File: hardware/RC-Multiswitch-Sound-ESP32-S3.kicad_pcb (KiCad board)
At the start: 2 copper layers, 124 x 60.1 mm, 37 parts, among them CN1 UART A, CN2 3S, CN4 Lautsprecher, J1 Ausgaenge, J11 TPA3118 HW-327, J2 PCM5102A, J5 UART B, J6 UART C, J9 microSD-TF-Modul, U1 ESP32-S3-DevKitC-1 (N16R8), U2 ULN2803A

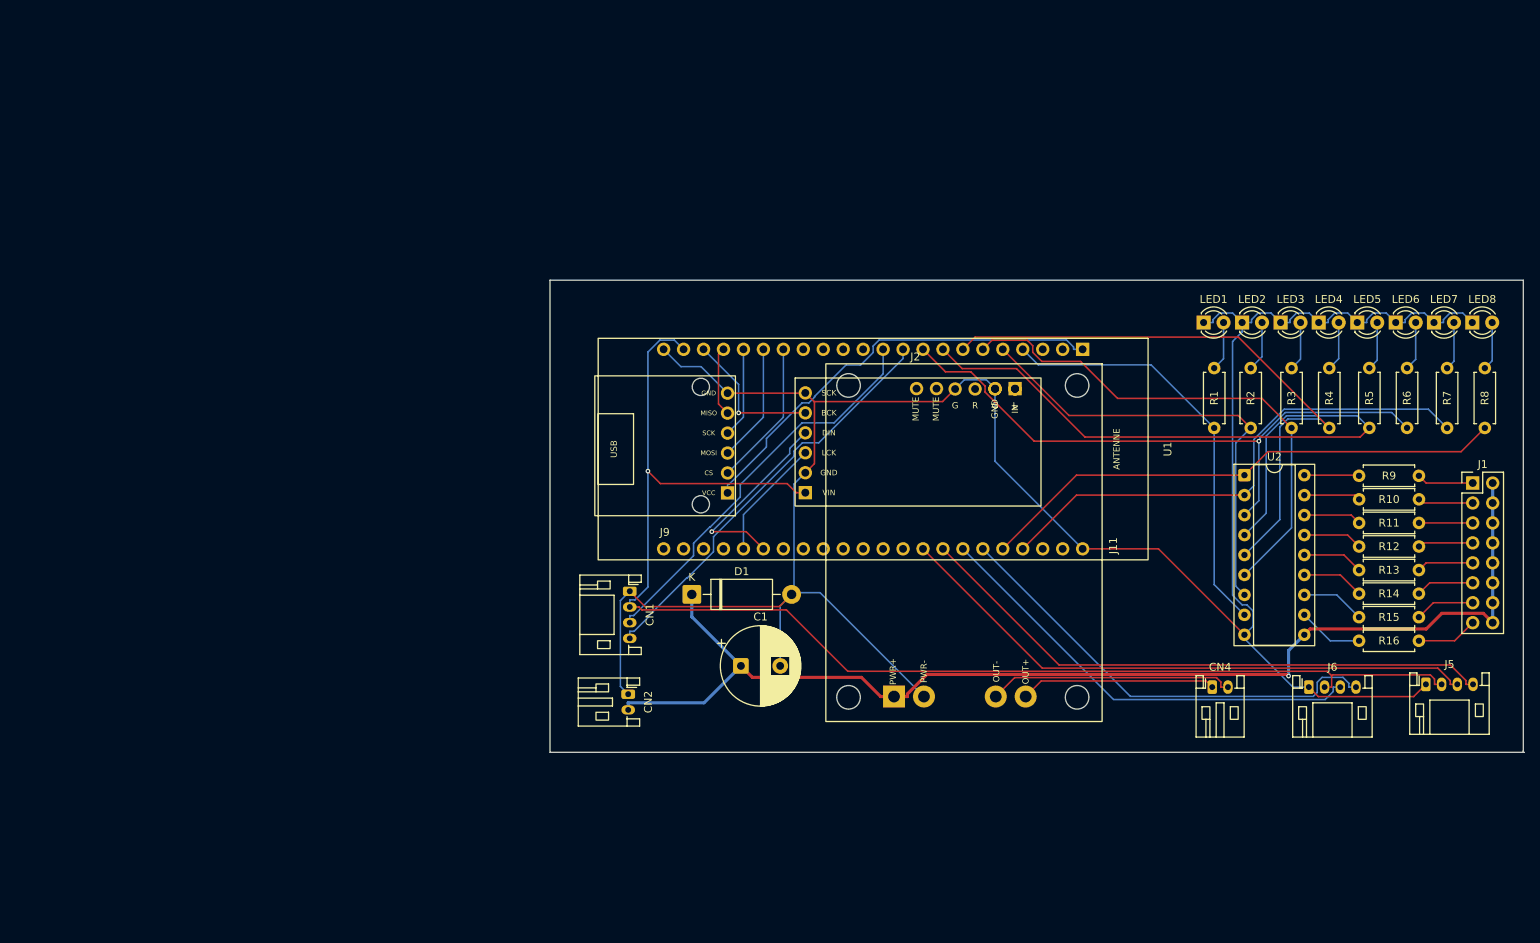
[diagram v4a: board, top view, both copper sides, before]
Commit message: PR #4 rückgängig: PCB wieder auf Stand vor VLOAD 0,4 mm
Auf Wunsch von Martin zurückgenommen.

Co-Authored-By: Claude Opus 5.5 (1M context) <noreply@anthropic.com>
Claude-Session: https://claude.ai/code/session_018bh1aktNNbeTvdMLiwxhbB
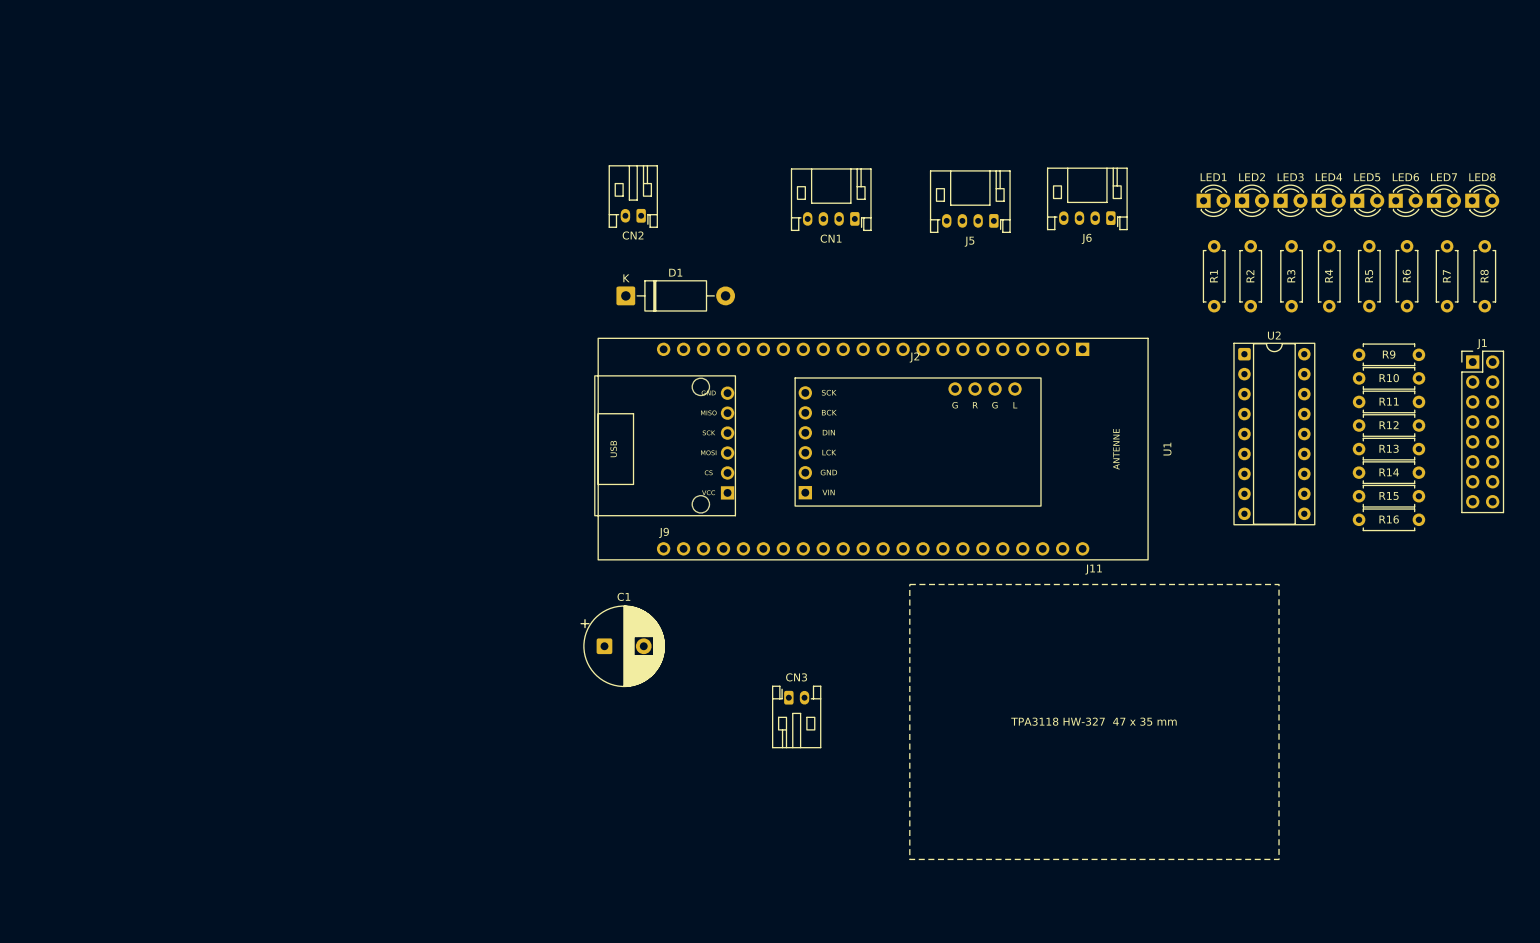
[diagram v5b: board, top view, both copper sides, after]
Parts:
- removed CN4: Lautsprecher, Connector_JST:JST_PH_S2B-PH-K_1x02_P2.00mm_Horizontal
- added CN3: TPA3118, Connector_JST:JST_PH_S2B-PH-K_1x02_P2.00mm_Horizontal, F.Cu at (176.2, 126.5)
- CN2: value 3S -> 12V
- D1: value P6KE15A -> P6KE33A
- J11: value TPA3118 HW-327 -> TPA3118 IN; footprint ESP32-S3-DevKitC-1_THT:Mod_TPA3118_HW327_THT -> ESP32-S3-DevKitC-1_THT:Mod_TPA3118_HW327_Keepout
- moved J5 80.7 mm to (202.3, 65.8), turned to 180 degrees
- moved J6 64.8 mm to (217.2, 65.4), turned to 180 degrees
- moved CN2 60.9 mm to (157.4, 65.1), turned to 180 degrees
- moved CN1 55.4 mm to (184.6, 65.5), turned to 180 degrees
- moved J11 43.6 mm to (215.1, 129.5), turned to 0 degrees
- moved D1 38.9 mm to (155.4, 75.3)
- moved C1 17.5 mm to (152.7, 119.9)
- moved LED1 15.5 mm to (229.0, 63.2)
- moved LED2 15.5 mm to (233.9, 63.2)
- moved LED3 15.5 mm to (238.8, 63.2)
- moved LED4 15.5 mm to (243.7, 63.2)
- moved LED5 15.5 mm to (248.6, 63.2)
- moved LED6 15.5 mm to (253.5, 63.2)
- moved LED7 15.5 mm to (258.3, 63.2)
- moved LED8 15.5 mm to (263.2, 63.2)
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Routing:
- net GND: track 302.5 -> 0.00 mm
- net +5V: track 170.9 -> 0.00 mm, vias 1 -> 0
- net /VLOAD: track 151.1 -> 0.00 mm, vias 1 -> 0
- net /S4: track 88.0 -> 0.00 mm
- net /S5: track 79.6 -> 0.00 mm, vias 1 -> 0
- net /S3: track 77.4 -> 0.00 mm
- net /UB_TX: track 75.5 -> 0.00 mm
- net /UB_RX: track 74.9 -> 0.00 mm
- net /S7: track 67.7 -> 0.00 mm
- net /S2: track 66.1 -> 0.00 mm
- net /S6: track 65.8 -> 0.00 mm
- net /S1: track 58.2 -> 0.00 mm
- net /UC_RX: track 57.9 -> 0.00 mm
- net /UC_TX: track 57.0 -> 0.00 mm
- net +3V3: track 55.8 -> 0.00 mm
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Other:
- board outline removed

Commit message: PCB: Platzierung/Routing von Martin (lokaler Stand), ERC-Bericht v0.9
Co-Authored-By: Claude Opus 5.5 (1M context) <noreply@anthropic.com>
Claude-Session: https://claude.ai/code/session_018bh1aktNNbeTvdMLiwxhbB
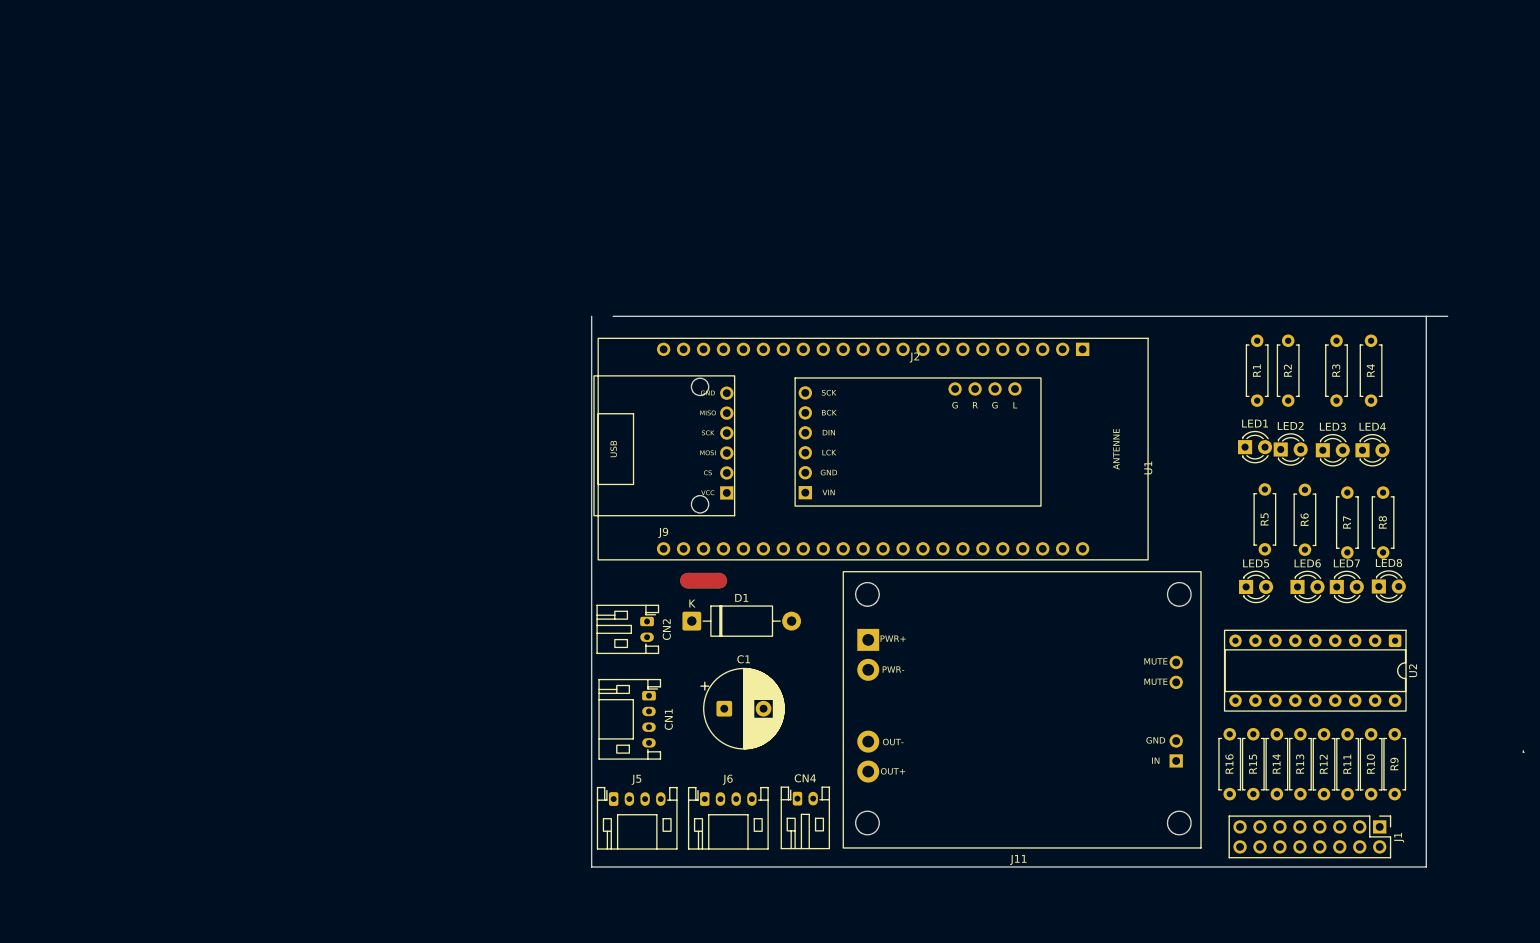
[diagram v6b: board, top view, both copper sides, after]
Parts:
- removed CN3: TPA3118, Connector_JST:JST_PH_S2B-PH-K_1x02_P2.00mm_Horizontal
- added CN4: Lautsprecher, Connector_JST:JST_PH_S2B-PH-K_1x02_P2.00mm_Horizontal, F.Cu at (177.3, 139.3)
- added NT1: NetTie GND/GNDPWR, NetTie:NetTie-2_SMD_Pad2.0mm, F.Cu at (165.3, 111.5)
- CN2: value 12V -> 3S
- D1: value P6KE33A -> P6KE15A
- J11: value TPA3118 IN -> TPA3118 HW-327; footprint ESP32-S3-DevKitC-1_THT:Mod_TPA3118_HW327_Keepout -> ESP32-S3-DevKitC-1_THT:Mod_TPA3118_HW327_THT
- moved J6 90.2 mm to (165.5, 139.3), turned to 0 degrees
- moved J5 88.1 mm to (153.9, 139.3), turned to 0 degrees
- moved CN1 66.1 mm to (158.4, 126.2), turned to -90 degrees
- moved J1 60.4 mm to (251.4, 142.9), turned to -90 degrees
- moved CN2 51.7 mm to (158.2, 116.8), turned to -90 degrees
- moved LED5 51.2 mm to (234.4, 112.3)
- moved LED6 50.7 mm to (241.0, 112.3)
- moved LED7 50.7 mm to (246.0, 112.3)
- moved LED8 50.5 mm to (251.3, 112.3)
- moved R9 48.5 mm to (253.3, 131.1), turned to -90 degrees
- moved R10 45.3 mm to (250.3, 131.1), turned to -90 degrees
- moved R11 42.3 mm to (247.3, 131.1), turned to -90 degrees
- moved D1 42.2 mm to (163.8, 116.7)
- moved U2 41.2 mm to (253.4, 119.2), turned to -90 degrees
- moved R12 39.6 mm to (244.3, 131.1), turned to -90 degrees
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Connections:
- U2 pad 9: GND -> GNDPWR
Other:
- board outline added: 118.7 x 70.1 mm

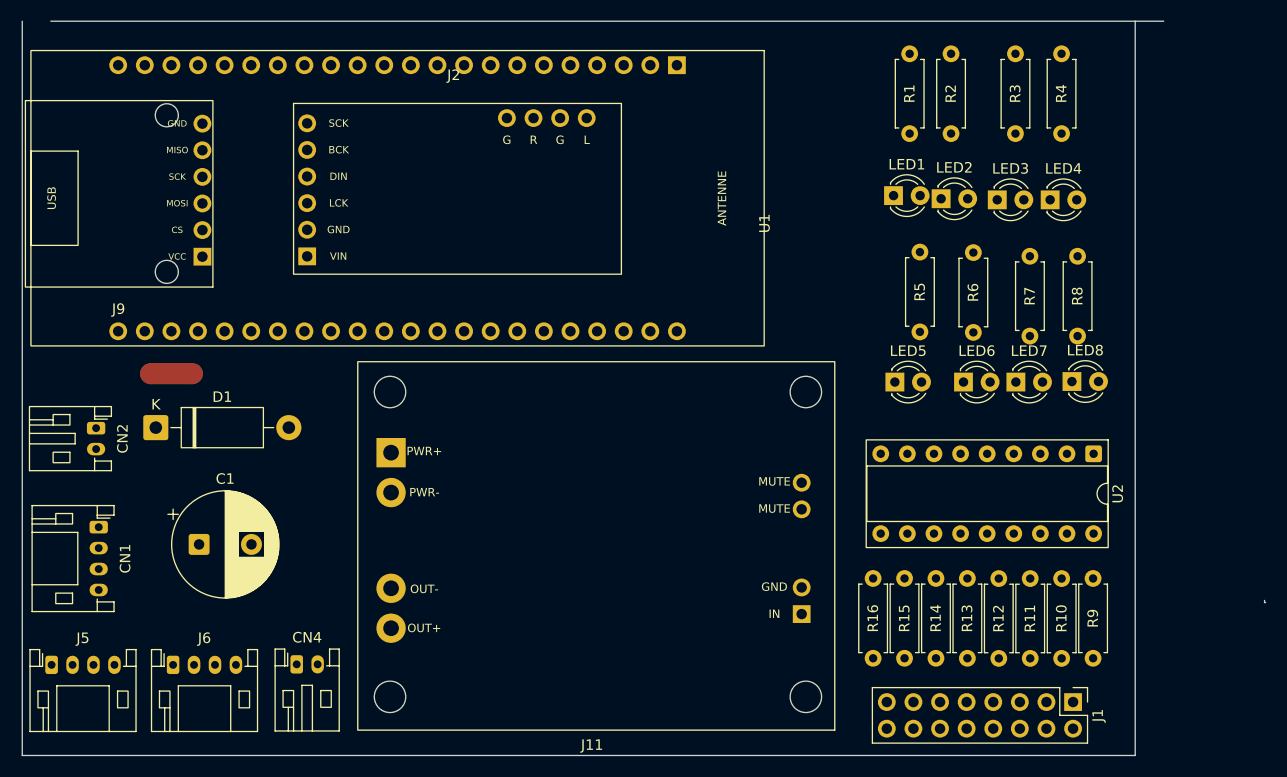
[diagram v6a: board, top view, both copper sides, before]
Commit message: PCB: Martins Stand 19.10. (Leiterbahnbreiten angepasst), DRC-Bericht
Co-Authored-By: Claude Opus 5.5 (1M context) <noreply@anthropic.com>
Claude-Session: https://claude.ai/code/session_018bh1aktNNbeTvdMLiwxhbB
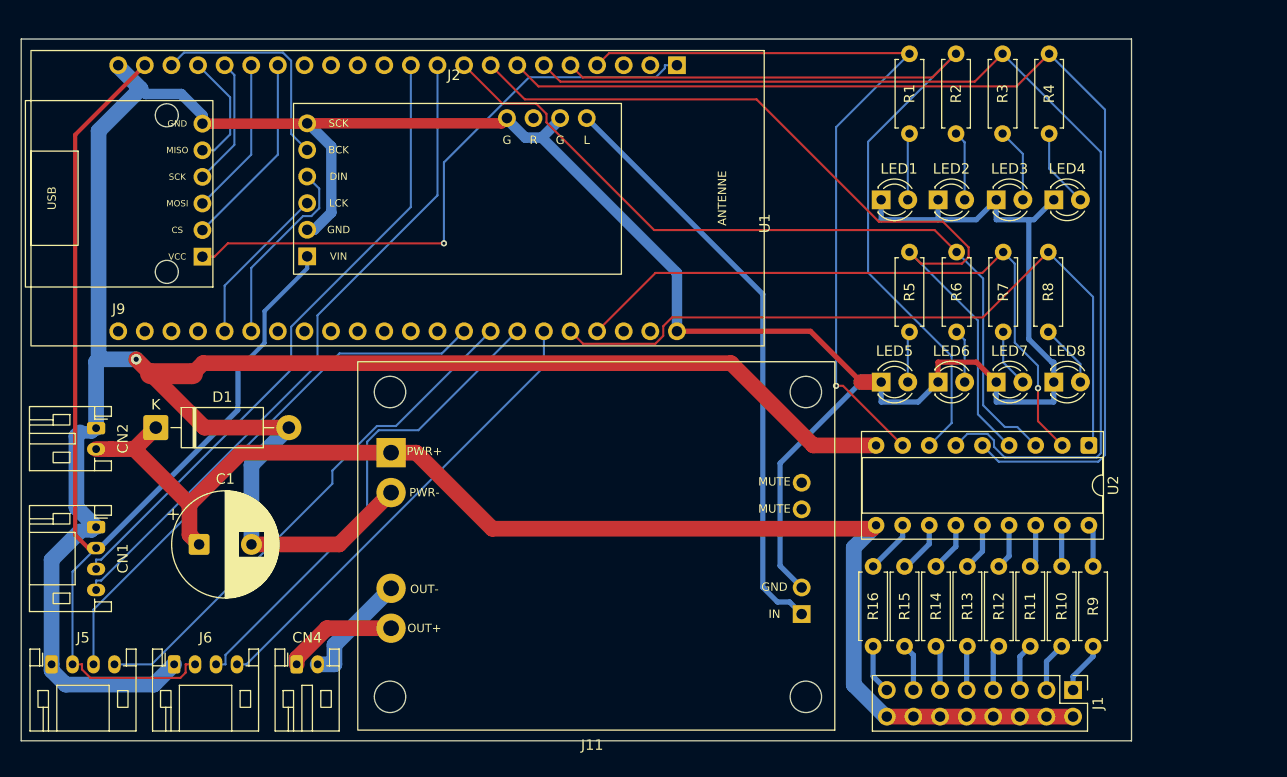
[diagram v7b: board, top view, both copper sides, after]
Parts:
- moved R8 2.83 mm to (249.1, 99.9)
- moved R7 2.58 mm to (244.8, 99.9)
- moved LED6 2.43 mm to (238.5, 112.3)
- moved LED7 1.87 mm to (244.1, 112.3)
- moved LED8 1.73 mm to (249.6, 112.3)
- moved R6 1.60 mm to (240.3, 99.9)
- moved LED5 1.31 mm to (233.1, 112.3)
- moved LED1 1.25 mm to (233.1, 95.0)
- moved R3 1.23 mm to (244.7, 81.0)
- moved R4 1.19 mm to (249.1, 81.0)
- moved R10 1.16 mm to (250.3, 129.9)
- moved R11 1.16 mm to (247.3, 129.9)
- moved R12 1.16 mm to (244.3, 129.9)
- moved J1 1.15 mm to (251.4, 141.8)
- moved R13 1.15 mm to (241.3, 129.9)
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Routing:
- net GND: track 0.00 -> 320.2 mm, vias 0 -> 1
- net /VLOAD: track 0.00 -> 127.3 mm
- net +5V: track 0.00 -> 112.5 mm
- net /S3: track 0.00 -> 106.0 mm
- net /S2: track 0.00 -> 103.3 mm
- net /S1: track 0.00 -> 83.3 mm
- net /S4: track 0.00 -> 82.5 mm
- net /S5: track 0.00 -> 77.2 mm
- net /S0: track 0.00 -> 73.6 mm, vias 0 -> 1
- net /S7: track 0.00 -> 70.7 mm
- net GNDPWR: track 0.00 -> 68.9 mm
- net /UA_TX: track 0.00 -> 63.9 mm
- net /S6: track 0.00 -> 62.7 mm, vias 0 -> 1
- net /UA_RX: track 0.00 -> 60.8 mm
- net +3V3: track 0.00 -> 57.6 mm, vias 0 -> 1
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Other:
- board size 118.7 x 70.1 mm -> 106 x 67 mm

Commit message: PCB: Martins Stand 20.10. 00:17, DRC-Bericht
Co-Authored-By: Claude Opus 5.5 (1M context) <noreply@anthropic.com>
Claude-Session: https://claude.ai/code/session_018bh1aktNNbeTvdMLiwxhbB
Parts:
- moved LED4 16.6 mm to (233.0, 94.3)
- moved LED8 16.6 mm to (233.0, 112.2)
- moved LED1 14.9 mm to (248.0, 94.3)
- moved LED5 14.9 mm to (248.0, 112.2)
- moved R4 14.9 mm to (234.3, 81.7)
- moved R8 14.8 mm to (234.3, 99.5)
- moved R1 13.5 mm to (249.3, 81.7)
- moved R5 13.5 mm to (249.3, 99.5)
- moved LED3 6.21 mm to (237.9, 94.3)
- moved LED7 6.18 mm to (237.9, 112.2)
- moved R7 5.58 mm to (239.2, 99.5)
- moved R3 5.49 mm to (239.2, 81.7)
- moved LED2 4.55 mm to (243.0, 94.3)
- moved LED6 4.50 mm to (243.0, 112.2)
- moved R2 4.17 mm to (244.3, 81.7)
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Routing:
- net /S0: track 73.6 -> 98.8 mm, vias 1 -> 0
- net /S1: track 83.3 -> 103.8 mm
- net +5V: track 112.5 -> 93.3 mm
- net /S2: track 103.3 -> 89.0 mm
- net /S5: track 77.2 -> 88.1 mm, vias 0 -> 1
- net /S3: track 106.0 -> 96.4 mm, vias 0 -> 1
- net /S7: track 70.7 -> 64.5 mm, vias 0 -> 1
- net +3V3: track 57.6 -> 53.3 mm
- net /S4: track 82.5 -> 86.3 mm, vias 0 -> 1
- net /UB_TX: track 52.2 -> 49.9 mm
- net /SD_MISO: track 11.2 -> 8.96 mm
- net Net-(LED4-A): track 7.56 -> 5.47 mm
- net /S6: track 62.7 -> 60.7 mm
- net Net-(LED3-A): track 7.12 -> 5.44 mm
- net GND: track 320.2 -> 318.6 mm
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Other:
- board size 106 x 67 mm -> 106 x 68.2 mm
- board text added: "+ -"
- board text added: "1"
- board text added: "2"
- board text added: "3"
- board text added: "4"
- board text added: "5"
- board text added: "6"
- board text added: "7"
- board text added: "8"
- board text added: "A (IN) TX RX + -"
- board text added: "ANTENNE"
- board text added: "B:- + TX RX"
- board text added: "C:- + TX RX"
- board text added: "CN2: 5V-12V"
- board text added: "ESP32-S3 (N16R8)"
- board text added: "LED1"
- board text added: "LED2"
- board text added: "LED3"
- board text added: "LED4"
- board text added: "LED5"
- board text added: "LED6"
- board text added: "LED7"
- board text added: "LED8"
- board text added: "Lautsprecher"
- board text added: "Micro-SD"
- board text added: "PCM5102A"
- board text added: "TPA3118"
- board text added: "ULN2803A"
